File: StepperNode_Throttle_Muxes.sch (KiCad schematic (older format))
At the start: 4 parts

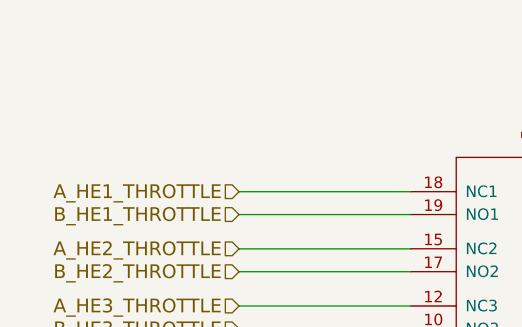
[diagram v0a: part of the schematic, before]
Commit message: Setup DAC channel B
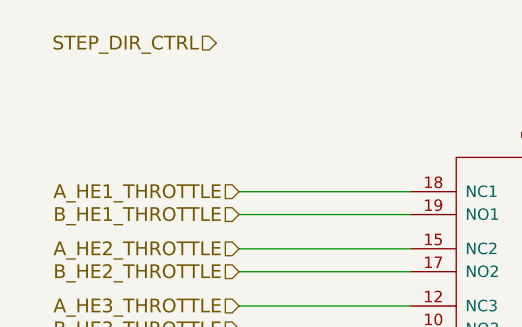
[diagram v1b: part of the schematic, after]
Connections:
- net labels added: STEP_DIR_CTRL
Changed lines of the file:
@@
 $Descr A3 16535 11693
 encoding utf-8
-Sheet 9 8
+Sheet 8 9
 Title "Throttle Multiplexers"
 Date ""
@@
 Text Notes 11750 6600 1    60   ~ 0
 Screened Cable with screen\nconnected to GND on PCB side\n1 Per RHS HE
+Text HLabel 5650 1550 0    60   Input ~ 0
+STEP_DIR_CTRL
 $EndSCHEMATC
